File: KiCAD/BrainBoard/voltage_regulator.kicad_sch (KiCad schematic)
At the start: 3 parts, among them U1 LM2940IMPX-5.0/NOPB

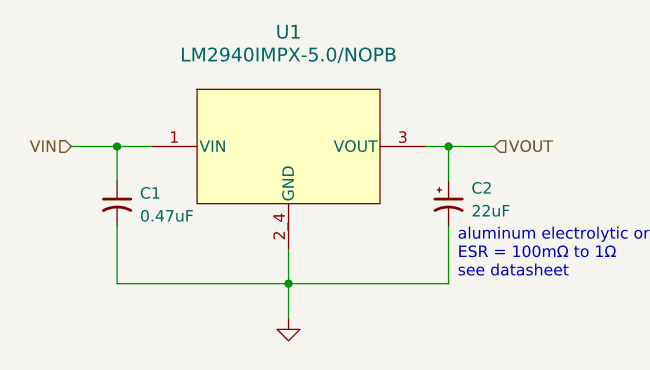
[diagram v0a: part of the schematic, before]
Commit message: [bug] make ERC happy
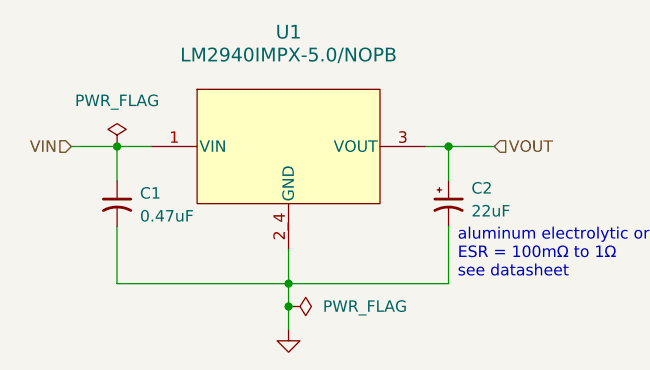
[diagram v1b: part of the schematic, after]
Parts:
- U1: footprint DCY0004A_N -> Project Footprints:LM2940IMPX_5.0NOPB
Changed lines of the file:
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@@
+	)
+	(junction
+		(at 138.43 111.76)
+		(diameter 0)
+		(color 0 0 0 0)
 	)
 	(junction
@@
 	(wire
 		(pts
+			(xy 138.43 111.76) (xy 138.43 109.22)
+		)
+		(stroke
+			(width 0)
+			(type default)
+		)
+	)
+	(wire
+		(pts
 			(xy 153.67 93.98) (xy 156.21 93.98)
 		)
@@
 	(wire
 		(pts
-			(xy 138.43 113.03) (xy 138.43 109.22)
+			(xy 138.43 114.3) (xy 138.43 111.76)
 		)
 		(stroke
@@
 	)
 	(symbol
+		(lib_id "power:PWR_FLAG")
+		(at 119.38 93.98 0)
+		(unit 1)
+		(exclude_from_sim no)
+		(in_bom yes)
+		(on_board yes)
+		(dnp no)
+		(fields_autoplaced yes)
+		(property "Reference" "#FLG01"
+			(at 119.38 92.075 0)
+			(effects
+				(font
+					(size 1.27 1.27)
+				)
+				(hide yes)
+			)
+		)
+		(property "Value" "PWR_FLAG"
+			(at 119.38 88.9 0)
+			(effects
+				(font
+					(size 1.27 1.27)
+				)
+			)
+		)
+		(property "Footprint" ""
+			(at 119.38 93.98 0)
+			(effects
+				(font
+					(size 1.27 1.27)
+				)
+				(hide yes)
+			)
+		)
+		(property "Datasheet" "~"
+			(at 119.38 93.98 0)
+			(effects
+				(font
+					(size 1.27 1.27)
+				)
+				(hide yes)
+			)
+		)
+		(property "Description" "Special symbol for telling ERC where power comes from"
+			(at 119.38 93.98 0)
+			(effects
+				(font
+					(size 1.27 1.27)
+				)
+				(hide yes)
+			)
+		)
+		(pin "1"
+		)
+		(instances
+			(project ""
+				(path "/44e391a9-9312-4881-bf0a-d93a44472e34/8dbe2292-b9b2-4749-8512-0e3dddbd3bdc"
+					(reference "#FLG01")
+					(unit 1)
+				)
+			)
+		)
+	)
+	(symbol
 		(lib_id "power:GND")
-		(at 138.43 113.03 0)
+		(at 138.43 114.3 0)
 		(unit 1)
 		(exclude_from_sim no)
@@
 		(fields_autoplaced yes)
 		(property "Reference" "#PWR01"
+			(at 138.43 120.65 0)
+			(effects
+				(font
+					(size 1.27 1.27)
+				)
+				(hide yes)
+			)
+		)
+		(property "Value" "GND"
 			(at 138.43 119.38 0)
 			(effects
@@
 			)
 		)
-		(property "Value" "GND"
-			(at 138.43 118.11 0)
-			(effects
-				(font
-					(size 1.27 1.27)
-				)
-				(hide yes)
-			)
-		)
 		(property "Footprint" ""
-			(at 138.43 113.03 0)
+			(at 138.43 114.3 0)
 			(effects
 				(font
@@
 		)
 		(property "Datasheet" ""
-			(at 138.43 113.03 0)
+			(at 138.43 114.3 0)
 			(effects
 				(font
@@
 		)
 		(property "Description" "Power symbol creates a global label with name \"GND\" , ground"
-			(at 138.43 113.03 0)
+			(at 138.43 114.3 0)
 			(effects
 				(font
@@
 		)
 		(instances
-			(project ""
-				(path "/44e391a9-9312-4881-bf0a-d93a44472e34/a7526b45-6acb-4529-b65f-9e79d8cdaf41"
+			(project "BrainBoard"
+				(path "/44e391a9-9312-4881-bf0a-d93a44472e34/8dbe2292-b9b2-4749-8512-0e3dddbd3bdc"
 					(reference "#PWR01")
 					(unit 1)
@@
 		)
 		(instances
-			(project ""
-				(path "/44e391a9-9312-4881-bf0a-d93a44472e34/a7526b45-6acb-4529-b65f-9e79d8cdaf41"
+			(project "BrainBoard"
+				(path "/44e391a9-9312-4881-bf0a-d93a44472e34/8dbe2292-b9b2-4749-8512-0e3dddbd3bdc"
 					(reference "C2")
 					(unit 1)
@@
 		)
 		(instances
-			(project ""
-				(path "/44e391a9-9312-4881-bf0a-d93a44472e34/a7526b45-6acb-4529-b65f-9e79d8cdaf41"
+			(project "BrainBoard"
+				(path "/44e391a9-9312-4881-bf0a-d93a44472e34/8dbe2292-b9b2-4749-8512-0e3dddbd3bdc"
 					(reference "C1")
+					(unit 1)
+				)
+			)
+		)
+	)
+	(symbol
+		(lib_id "power:PWR_FLAG")
+		(at 138.43 111.76 270)
+		(unit 1)
+		(exclude_from_sim no)
+		(in_bom yes)
+		(on_board yes)
+		(dnp no)
+		(fields_autoplaced yes)
+		(property "Reference" "#FLG02"
+			(at 140.335 111.76 0)
+			(effects
+				(font
+					(size 1.27 1.27)
+				)
+				(hide yes)
+			)
+		)
+		(property "Value" "PWR_FLAG"
+			(at 142.24 111.7599 90)
+			(effects
+				(font
+					(size 1.27 1.27)
+				)
+				(justify left)
+			)
+		)
+		(property "Footprint" ""
+			(at 138.43 111.76 0)
+			(effects
+				(font
+					(size 1.27 1.27)
+				)
+				(hide yes)
+			)
+		)
+		(property "Datasheet" "~"
+			(at 138.43 111.76 0)
+			(effects
+				(font
+					(size 1.27 1.27)
+				)
+				(hide yes)
+			)
+		)
+		(property "Description" "Special symbol for telling ERC where power comes from"
+			(at 138.43 111.76 0)
+			(effects
+				(font
+					(size 1.27 1.27)
+				)
+				(hide yes)
+			)
+		)
+		(pin "1"
+		)
+		(instances
+			(project "BrainBoard"
+				(path "/44e391a9-9312-4881-bf0a-d93a44472e34/8dbe2292-b9b2-4749-8512-0e3dddbd3bdc"
+					(reference "#FLG02")
 					(unit 1)
 				)
@@
 			)
 		)
-		(property "Footprint" "DCY0004A_N"
+		(property "Footprint" "Project Footprints:LM2940IMPX_5.0NOPB"
 			(at 138.43 93.98 0)
 			(effects
@@
 		)
 		(instances
-			(project ""
-				(path "/44e391a9-9312-4881-bf0a-d93a44472e34/a7526b45-6acb-4529-b65f-9e79d8cdaf41"
+			(project "BrainBoard"
+				(path "/44e391a9-9312-4881-bf0a-d93a44472e34/8dbe2292-b9b2-4749-8512-0e3dddbd3bdc"
 					(reference "U1")
 					(unit 1)

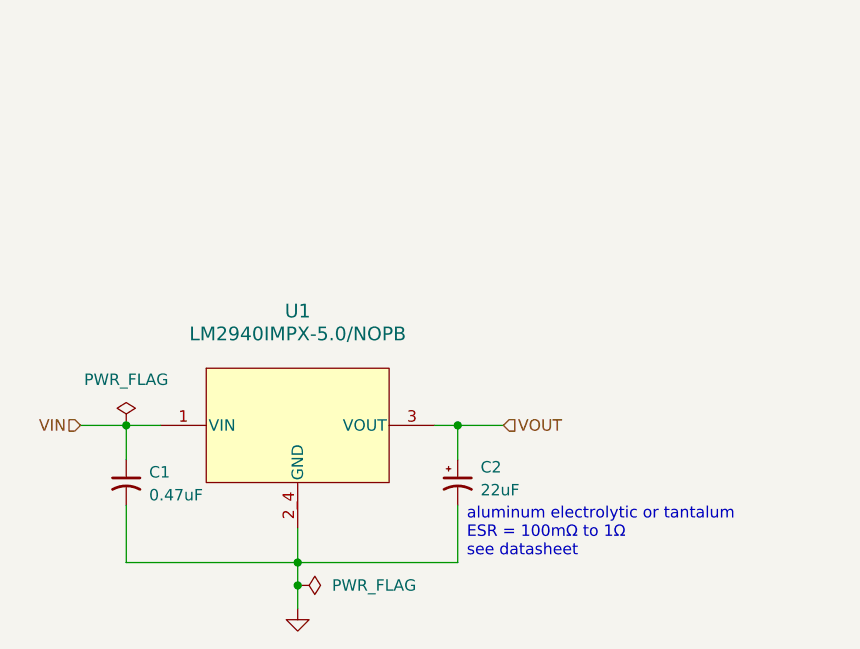
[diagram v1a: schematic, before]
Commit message: [feat] add example motor driver
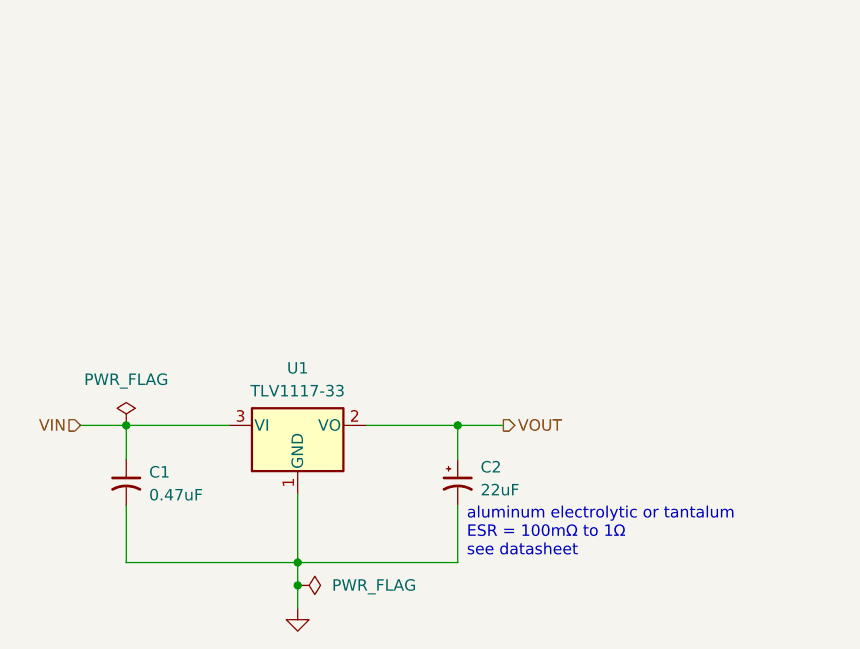
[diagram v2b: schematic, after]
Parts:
- removed U1: LM2940IMPX-5.0/NOPB, Project Footprints:LM2940IMPX_5.0NOPB, symbol LM2940IMPX_5.0NOPB:LM2940IMPX-5.0_NOPB
- added U1: TLV1117-33, symbol Regulator_Linear:TLV1117-33
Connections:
- net GND: now also U1.1 (GND)
- net VIN: now also U1.3 (VI)
- net VOUT: now also U1.2 (VO)
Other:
- company: (none) -> Nathan Wignall
- title: (none) -> Voltage Regulator
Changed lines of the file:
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@@
 	(generator_version "9.0")
 	(paper "A4")
+	(title_block
+		(title "Voltage Regulator")
+		(date "${CURRENT_DATE}")
+		(company "Nathan Wignall")
+	)
 	(text "aluminum electrolytic or tantalum\nESR = 100mΩ to 1Ω\nsee datasheet"
 		(exclude_from_sim no)
@@
 	(wire
 		(pts
-			(xy 153.67 93.98) (xy 156.21 93.98)
-		)
-		(stroke
-			(width 0)
-			(type default)
-		)
-	)
-	(wire
-		(pts
 			(xy 114.3 93.98) (xy 119.38 93.98)
 		)
@@
 	(wire
 		(pts
-			(xy 119.38 93.98) (xy 123.19 93.98)
+			(xy 119.38 93.98) (xy 130.81 93.98)
 		)
 		(stroke
@@
 	(wire
 		(pts
-			(xy 138.43 109.22) (xy 138.43 105.41)
+			(xy 146.05 93.98) (xy 156.21 93.98)
+		)
+		(stroke
+			(width 0)
+			(type default)
+		)
+	)
+	(wire
+		(pts
+			(xy 138.43 101.6) (xy 138.43 109.22)
 		)
 		(stroke
@@
 	)
 	(hierarchical_label "VOUT"
-		(shape input)
+		(shape output)
 		(at 161.29 93.98 0)
 		(effects
@@
 			)
 			(justify left)
+		)
+	)
+	(symbol
+		(lib_id "Regulator_Linear:TLV1117-33")
+		(at 138.43 93.98 0)
+		(unit 1)
+		(exclude_from_sim no)
+		(in_bom yes)
+		(on_board yes)
+		(dnp no)
+		(fields_autoplaced yes)
+		(property "Reference" "U1"
+			(at 138.43 87.63 0)
+			(effects
+				(font
+					(size 1.27 1.27)
+				)
+			)
+		)
+		(property "Value" "TLV1117-33"
+			(at 138.43 90.17 0)
+			(effects
+				(font
+					(size 1.27 1.27)
+				)
+			)
+		)
+		(property "Footprint" ""
+			(at 138.43 93.98 0)
+			(effects
+				(font
+					(size 1.27 1.27)
+				)
+				(hide yes)
+			)
+		)
+		(property "Datasheet" "http://www.ti.com/lit/ds/symlink/tlv1117.pdf"
+			(at 138.43 93.98 0)
+			(effects
+				(font
+					(size 1.27 1.27)
+				)
+				(hide yes)
+			)
+		)
+		(property "Description" "800mA Low-Dropout Linear Regulator, 3.3V fixed output, TO-220/TO-252/TO-263/SOT-223"
+			(at 138.43 93.98 0)
+			(effects
+				(font
+					(size 1.27 1.27)
+				)
+				(hide yes)
+			)
+		)
+		(pin "3"
+		)
+		(pin "1"
+		)
+		(pin "2"
+		)
+		(instances
+			(project ""
+				(path "/44e391a9-9312-4881-bf0a-d93a44472e34/8dbe2292-b9b2-4749-8512-0e3dddbd3bdc"
+					(reference "U1")
+					(unit 1)
+				)
+			)
 		)
 	)
@@
 					(unit 1)
 				)
-			)
-		)
-	)
-	(symbol
-		(lib_id "LM2940IMPX_5.0NOPB:LM2940IMPX-5.0_NOPB")
-		(at 138.43 93.98 0)
-		(unit 1)
-		(exclude_from_sim no)
-		(in_bom yes)
-		(on_board yes)
-		(dnp no)
-		(fields_autoplaced yes)
-		(property "Reference" "U1"
-			(at 138.43 81.28 0)
-			(effects
-				(font
-					(size 1.524 1.524)
-				)
-			)
-		)
-		(property "Value" "LM2940IMPX-5.0/NOPB"
-			(at 138.43 83.82 0)
-			(effects
-				(font
-					(size 1.524 1.524)
-				)
-			)
-		)
-		(property "Footprint" "Project Footprints:LM2940IMPX_5.0NOPB"
-			(at 138.43 93.98 0)
-			(effects
-				(font
-					(size 1.27 1.27)
-					(italic yes)
-				)
-				(hide yes)
-			)
-		)
-		(property "Datasheet" "https://www.ti.com/lit/gpn/lm2940-n"
-			(at 138.43 93.98 0)
-			(effects
-				(font
-					(size 1.27 1.27)
-					(italic yes)
-				)
-				(hide yes)
-			)
-		)
-		(property "Description" ""
-			(at 138.43 93.98 0)
-			(effects
-				(font
-					(size 1.27 1.27)
-				)
-				(hide yes)
-			)
-		)
-		(pin "3"
-		)
-		(pin "1"
-		)
-		(pin "2_4"
-		)
-		(instances
-			(project "BrainBoard"
-				(path "/44e391a9-9312-4881-bf0a-d93a44472e34/8dbe2292-b9b2-4749-8512-0e3dddbd3bdc"
-					(reference "U1")
-					(unit 1)
-				)

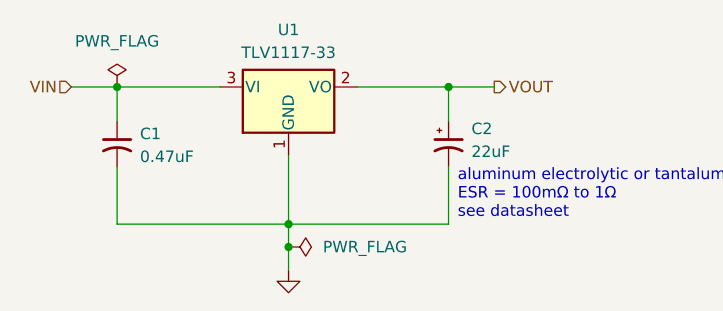
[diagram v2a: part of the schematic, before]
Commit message: [feature] Finalize DRV8231DSGR motor drivers
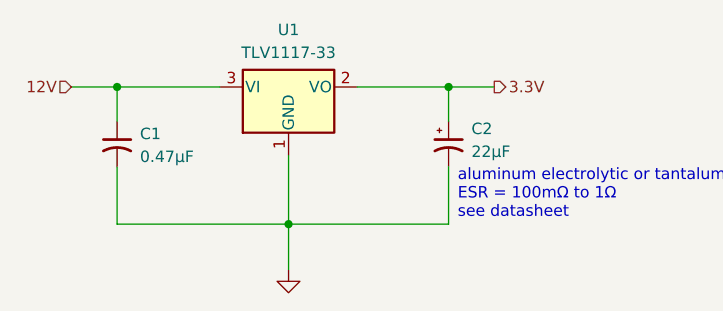
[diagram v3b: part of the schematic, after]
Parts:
- C1: value 0.47uF -> 0.47µF
- C2: value 22uF -> 22µF
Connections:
- net VIN renamed 12V
- net VOUT renamed 3.3V
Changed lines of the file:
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@@
-	)
-	(junction
-		(at 138.43 111.76)
-		(diameter 0)
-		(color 0 0 0 0)
 	)
 	(junction
@@
 	(wire
 		(pts
-			(xy 138.43 111.76) (xy 138.43 109.22)
+			(xy 138.43 109.22) (xy 138.43 114.3)
 		)
 		(stroke
@@
 	(wire
 		(pts
-			(xy 138.43 114.3) (xy 138.43 111.76)
-		)
-		(stroke
-			(width 0)
-			(type default)
-		)
-	)
-	(wire
-		(pts
 			(xy 156.21 93.98) (xy 161.29 93.98)
 		)
@@
 		)
 	)
-	(hierarchical_label "VIN"
+	(hierarchical_label "12V"
 		(shape input)
 		(at 114.3 93.98 180)
@@
 		)
 	)
-	(hierarchical_label "VOUT"
+	(hierarchical_label "3.3V"
 		(shape output)
 		(at 161.29 93.98 0)
@@
 	)
 	(symbol
-		(lib_id "power:PWR_FLAG")
-		(at 119.38 93.98 0)
-		(unit 1)
-		(exclude_from_sim no)
-		(in_bom yes)
-		(on_board yes)
-		(dnp no)
-		(fields_autoplaced yes)
-		(property "Reference" "#FLG01"
-			(at 119.38 92.075 0)
-			(effects
-				(font
-					(size 1.27 1.27)
-				)
-				(hide yes)
-			)
-		)
-		(property "Value" "PWR_FLAG"
-			(at 119.38 88.9 0)
-			(effects
-				(font
-					(size 1.27 1.27)
-				)
-			)
-		)
-		(property "Footprint" ""
-			(at 119.38 93.98 0)
-			(effects
-				(font
-					(size 1.27 1.27)
-				)
-				(hide yes)
-			)
-		)
-		(property "Datasheet" "~"
-			(at 119.38 93.98 0)
-			(effects
-				(font
-					(size 1.27 1.27)
-				)
-				(hide yes)
-			)
-		)
-		(property "Description" "Special symbol for telling ERC where power comes from"
-			(at 119.38 93.98 0)
-			(effects
-				(font
-					(size 1.27 1.27)
-				)
-				(hide yes)
-			)
-		)
-		(pin "1"
-		)
-		(instances
-			(project ""
-				(path "/44e391a9-9312-4881-bf0a-d93a44472e34/8dbe2292-b9b2-4749-8512-0e3dddbd3bdc"
-					(reference "#FLG01")
-					(unit 1)
-				)
-			)
-		)
-	)
-	(symbol
 		(lib_id "power:GND")
 		(at 138.43 114.3 0)
@@
 			)
 		)
-		(property "Value" "22uF"
+		(property "Value" "22µF"
 			(at 158.75 101.1681 0)
 			(effects
@@
 			)
 		)
-		(property "Value" "0.47uF"
+		(property "Value" "0.47µF"
 			(at 121.92 101.7269 0)
 			(effects
@@
 					(unit 1)
 				)
-			)
-		)
-	)
-	(symbol
-		(lib_id "power:PWR_FLAG")
-		(at 138.43 111.76 270)
-		(unit 1)
-		(exclude_from_sim no)
-		(in_bom yes)
-		(on_board yes)
-		(dnp no)
-		(fields_autoplaced yes)
-		(property "Reference" "#FLG02"
-			(at 140.335 111.76 0)
-			(effects
-				(font
-					(size 1.27 1.27)
-				)
-				(hide yes)
-			)
-		)
-		(property "Value" "PWR_FLAG"
-			(at 142.24 111.7599 90)
-			(effects
-				(font
-					(size 1.27 1.27)
-				)
-				(justify left)
-			)
-		)
-		(property "Footprint" ""
-			(at 138.43 111.76 0)
-			(effects
-				(font
-					(size 1.27 1.27)
-				)
-				(hide yes)
-			)
-		)
-		(property "Datasheet" "~"
-			(at 138.43 111.76 0)
-			(effects
-				(font
-					(size 1.27 1.27)
-				)
-				(hide yes)
-			)
-		)
-		(property "Description" "Special symbol for telling ERC where power comes from"
-			(at 138.43 111.76 0)
-			(effects
-				(font
-					(size 1.27 1.27)
-				)
-				(hide yes)
-			)
-		)
-		(pin "1"
-		)
-		(instances
-			(project "BrainBoard"
-				(path "/44e391a9-9312-4881-bf0a-d93a44472e34/8dbe2292-b9b2-4749-8512-0e3dddbd3bdc"
-					(reference "#FLG02")
-					(unit 1)
-				)

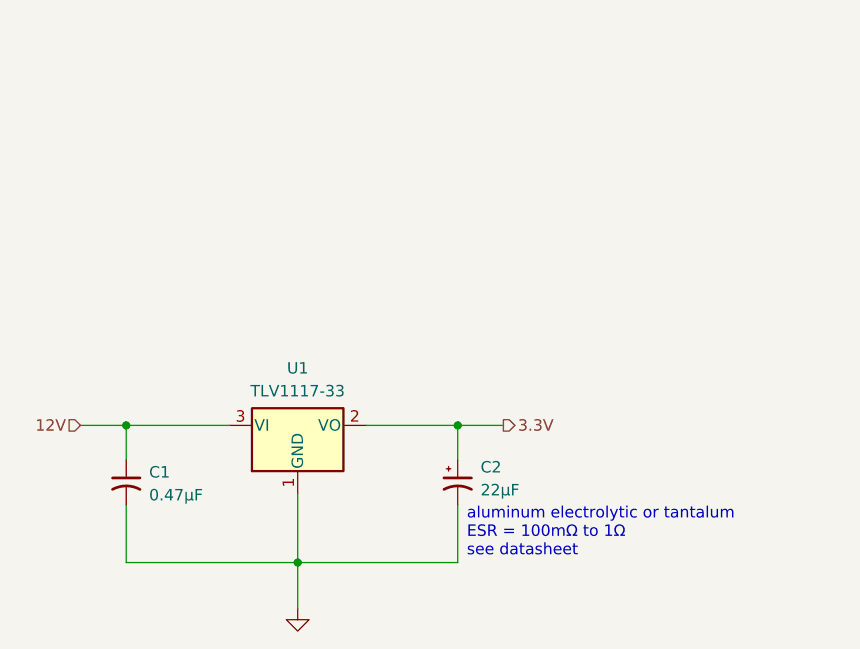
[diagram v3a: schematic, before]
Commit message: feat: battery input
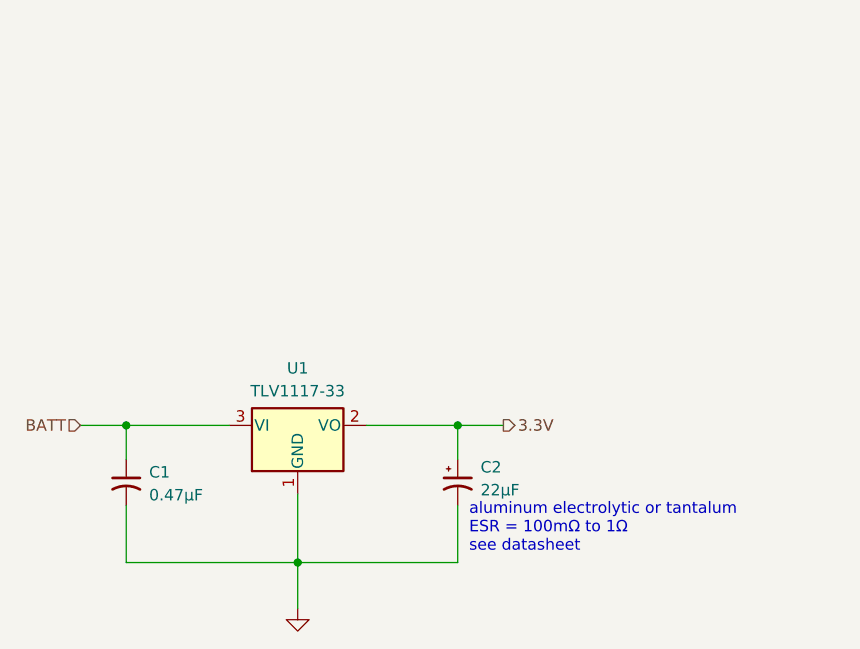
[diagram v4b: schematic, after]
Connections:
- net 12V renamed BATT
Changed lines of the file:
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@@
 	(text "aluminum electrolytic or tantalum\nESR = 100mΩ to 1Ω\nsee datasheet"
 		(exclude_from_sim no)
-		(at 157.226 105.918 0)
+		(at 157.48 105.41 0)
 		(effects
 			(font
@@
 		)
 	)
-	(hierarchical_label "12V"
+	(hierarchical_label "BATT"
 		(shape input)
 		(at 114.3 93.98 180)

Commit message: feat: add +5V line
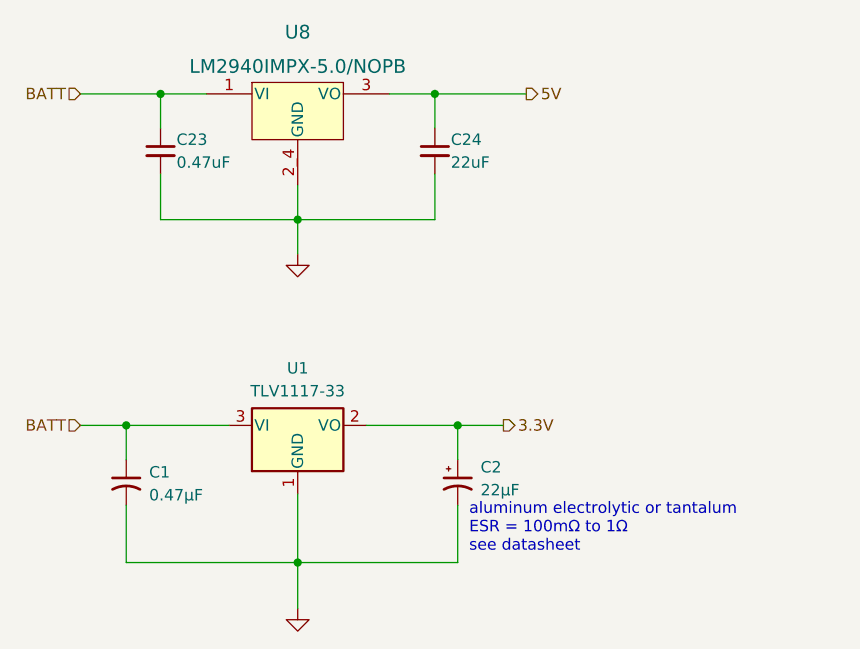
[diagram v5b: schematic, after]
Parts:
- added C23: 0.47uF, Capacitor_SMD:C_1206_3216Metric, symbol Device:C_Small
- added C24: 22uF, Capacitor_SMD:C_1206_3216Metric, symbol Device:C_Small
- added U8: LM2940IMPX-5.0/NOPB, footprints:DCY0004A_N, symbol LM2940IMPX-5:LM2940IMPX-5.0_NOPB
- U1: footprint (none) -> footprints:DCY0004A_N
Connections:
- net BATT: now also C23.1, U8.1 (VI)
- net GND: now also C23.2, C24.2, U8.2_4 (GND)
- new net 5V: C24.1, U8.3 (VO)

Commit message: Assigned most general footprints
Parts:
- C1: footprint (none) -> Capacitor_SMD:C_0805_2012Metric
- C23: footprint Capacitor_SMD:C_1206_3216Metric -> Capacitor_SMD:C_0805_2012Metric
- C24: footprint Capacitor_SMD:C_1206_3216Metric -> (none)
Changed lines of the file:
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@@
 			)
 		)
-		(property "Footprint" ""
+		(property "Footprint" "Capacitor_SMD:C_0805_2012Metric"
 			(at 119.38 100.33 0)
 			(effects
@@
 			)
 		)
-		(property "Footprint" "Capacitor_SMD:C_1206_3216Metric"
+		(property "Footprint" ""
 			(at 153.67 63.5 0)
 			(effects
@@
 			)
 		)
-		(property "Footprint" "Capacitor_SMD:C_1206_3216Metric"
+		(property "Footprint" "Capacitor_SMD:C_0805_2012Metric"
 			(at 123.19 63.5 0)
 			(effects
